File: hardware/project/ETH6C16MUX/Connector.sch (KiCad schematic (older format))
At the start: 3 parts, among them J701 Conn_01x06, J702 Conn_02x09_Odd_Even, J703 C64AC

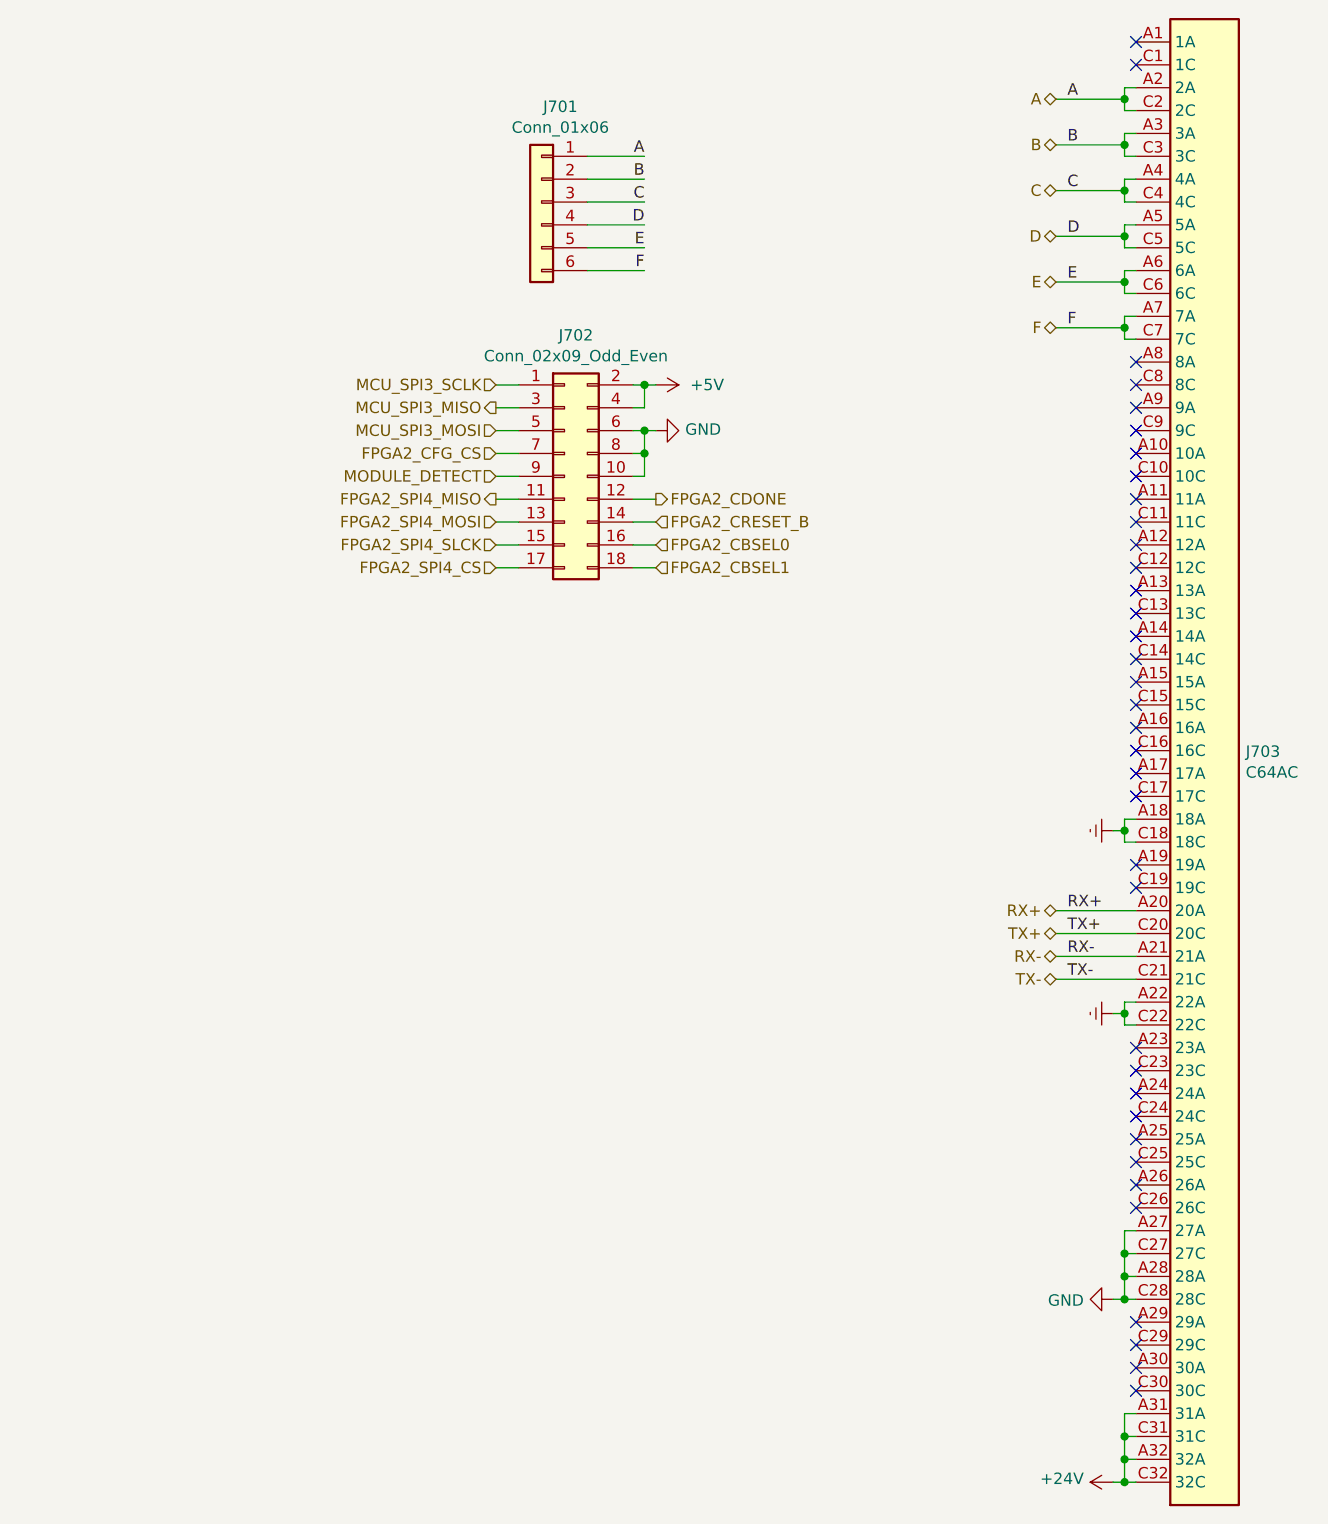
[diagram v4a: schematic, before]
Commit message: Deleted FPGA part and change it for SPI IO chips. Change power supply circuit.
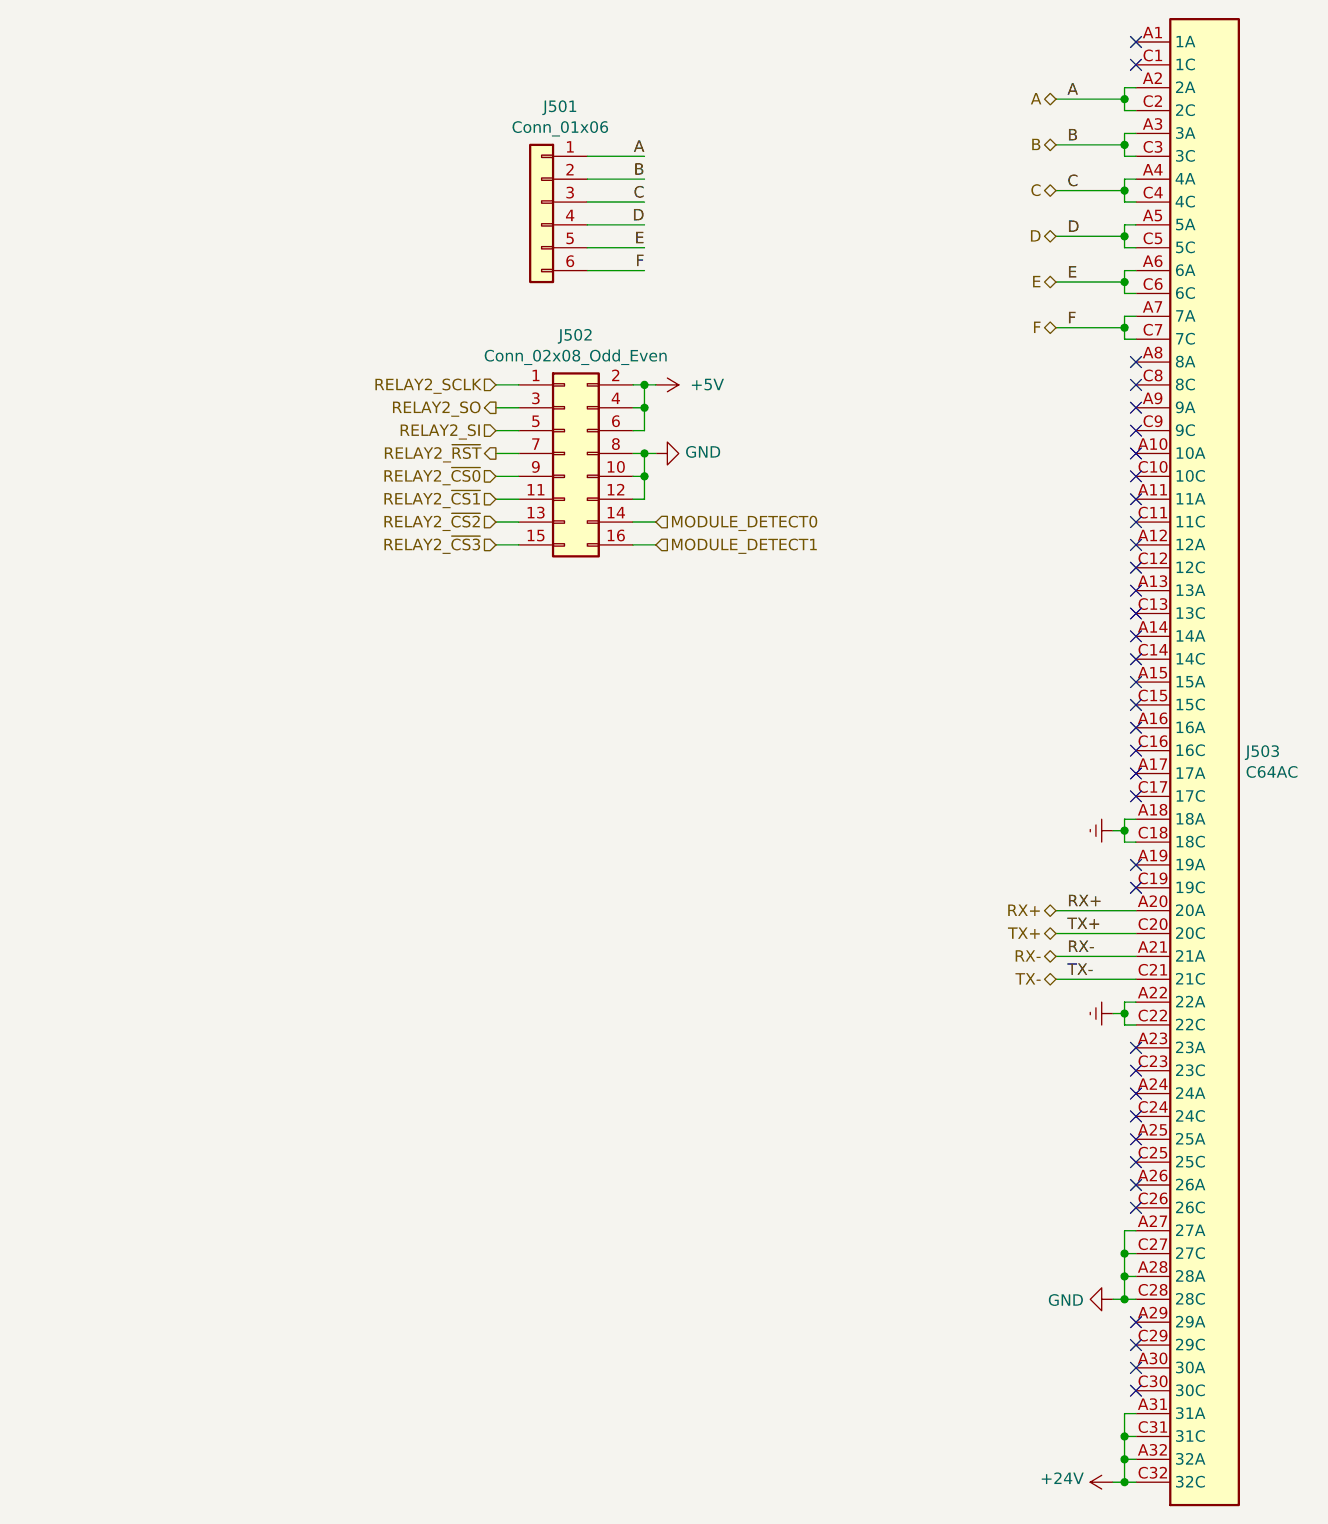
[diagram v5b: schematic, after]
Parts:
- removed J702: Conn_02x09_Odd_Even, Connector_PinSocket_2.54mm:PinSocket_2x09_P2.54mm_Vertical, symbol Connector_Generic:Conn_02x09_Odd_Even
- added J502: Conn_02x08_Odd_Even, Connector_PinSocket_2.54mm:PinSocket_2x08_P2.54mm_Vertical, symbol Connector_Generic:Conn_02x08_Odd_Even
- renumbered J701 to J501, J703 to J503
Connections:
- net +5V: now also J502.2 (Pin_2), J502.4 (Pin_4), J502.6 (Pin_6)
- net GND: now also J502.10 (Pin_10), J502.12 (Pin_12), J502.8 (Pin_8)
- new net MODULE_DETECT0: J502.14 (Pin_14)
- new net MODULE_DETECT1: J502.16 (Pin_16)
- new net RELAY2_SCLK: J502.1 (Pin_1)
- new net RELAY2_SI: J502.5 (Pin_5)
- new net RELAY2_SO: J502.3 (Pin_3)
- new net RELAY2_~CS0: J502.9 (Pin_9)
- new net RELAY2_~CS1: J502.11 (Pin_11)
- new net RELAY2_~CS2: J502.13 (Pin_13)
- new net RELAY2_~CS3: J502.15 (Pin_15)
- new net RELAY2_~RST: J502.7 (Pin_7)
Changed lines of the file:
@@
 $Descr A4 11693 8268
 encoding utf-8
-Sheet 7 7
+Sheet 5 6
 Title ""
 Date ""
@@
 $EndDescr
 $Comp
-L Connector:C64AC J703
+L Connector:C64AC J503
 U 1 1 5DB3A84B
 P 5950 4000
-F 0 "J703" H 6130 4096 50  0000 L CNN
+F 0 "J503" H 6130 4096 50  0000 L CNN
 F 1 "C64AC" H 6130 4005 50  0000 L CNN
 F 2 "ETH6C16MXU:Socket_DIN41612-CaseC1-AC-Male-64Pin-2rows" H 5950 4050 50  0001 C CNN
@@
 	5600 6200 5600 6100
 $Comp
-L power:+24V #PWR0706
+L power:+24V #PWR0506
 U 1 1 5D7D1F7C
 P 5550 7100
-F 0 "#PWR0706" H 5550 6950 50  0001 C CNN
+F 0 "#PWR0506" H 5550 6950 50  0001 C CNN
 F 1 "+24V" V 5565 7228 50  0000 L CNN
 F 2 "" H 5550 7100 50  0001 C CNN
@@
 Connection ~ 5600 7100
 $Comp
-L power:GND #PWR0705
+L power:GND #PWR0505
 U 1 1 5D7D46BE
 P 5550 6300
-F 0 "#PWR0705" H 5550 6050 50  0001 C CNN
+F 0 "#PWR0505" H 5550 6050 50  0001 C CNN
 F 1 "GND" V 5555 6172 50  0000 R CNN
 F 2 "" H 5550 6300 50  0001 C CNN
@@
 RX-
 $Comp
-L power:Earth #PWR0704
+L power:Earth #PWR0504
 U 1 1 5D7F1666
 P 5550 5050
-F 0 "#PWR0704" H 5550 4800 50  0001 C CNN
+F 0 "#PWR0504" H 5550 4800 50  0001 C CNN
 F 1 "Earth" H 5550 4900 50  0001 C CNN
 F 2 "" H 5550 5050 50  0001 C CNN
@@
 	5600 5050 5600 5000
 $Comp
-L power:Earth #PWR0703
+L power:Earth #PWR0503
 U 1 1 5D7F6C0C
 P 5550 4250
-F 0 "#PWR0703" H 5550 4000 50  0001 C CNN
+F 0 "#PWR0503" H 5550 4000 50  0001 C CNN
 F 1 "Earth" H 5550 4100 50  0001 C CNN
 F 2 "" H 5550 4250 50  0001 C CNN
@@
 F
 Wire Wire Line
-	3550 2500 3500 2500
+	3550 2600 3500 2600
+Wire Wire Line
+	3450 2700 3500 2700
+Wire Wire Line
+	3500 2600 3500 2700
+Connection ~ 3500 2600
 Wire Wire Line
 	3450 2600 3500 2600
-Wire Wire Line
-	3500 2500 3500 2600
-Connection ~ 3500 2500
-Wire Wire Line
-	3450 2500 3500 2500
 Wire Wire Line
 	3500 2300 3550 2300
@@
 	2950 2800 2850 2800
 Wire Wire Line
-	2850 3100 2950 3100
-Wire Wire Line
-	2950 3000 2850 3000
-Wire Wire Line
 	2850 2600 2950 2600
 Wire Wire Line
-	3450 3100 3550 3100
-Wire Wire Line
 	3550 3000 3450 3000
 Wire Wire Line
 	3550 2900 3450 2900
 Wire Wire Line
-	3550 2800 3450 2800
-Wire Wire Line
 	2950 2500 2850 2500
 Wire Wire Line
@@
 Wire Wire Line
 	2950 2300 2850 2300
-Text HLabel 2850 2700 0    50   Input ~ 0
-MODULE_DETECT
-$Comp
-L power:GND #PWR0702
+$Comp
+L power:GND #PWR0502
 U 1 1 5D777B58
-P 3550 2500
-AR Path="/5DB25E5A/5D777B58" Ref="#PWR0702"  Part="1"
+P 3550 2600
+AR Path="/5DB25E5A/5D777B58" Ref="#PWR0502"  Part="1"
 AR Path="/5D7599BA/5D777B58" Ref="#PWR?"  Part="1"
-F 0 "#PWR0702" H 3550 2250 50  0001 C CNN
-F 1 "GND" V 3555 2372 50  0000 R CNN
-F 2 "" H 3550 2500 50  0001 C CNN
-F 3 "" H 3550 2500 50  0001 C CNN
-	1    3550 2500
+F 0 "#PWR0502" H 3550 2350 50  0001 C CNN
+F 1 "GND" V 3555 2472 50  0000 R CNN
+F 2 "" H 3550 2600 50  0001 C CNN
+F 3 "" H 3550 2600 50  0001 C CNN
+	1    3550 2600
 	0    -1   -1   0
 $EndComp
 $Comp
-L power:+5V #PWR0701
+L power:+5V #PWR0501
 U 1 1 5D777B5E
 P 3550 2300
-AR Path="/5DB25E5A/5D777B5E" Ref="#PWR0701"  Part="1"
+AR Path="/5DB25E5A/5D777B5E" Ref="#PWR0501"  Part="1"
 AR Path="/5D7599BA/5D777B5E" Ref="#PWR?"  Part="1"
-F 0 "#PWR0701" H 3550 2150 50  0001 C CNN
+F 0 "#PWR0501" H 3550 2150 50  0001 C CNN
 F 1 "+5V" V 3550 2450 50  0000 L CNN
 F 2 "" H 3550 2300 50  0001 C CNN
@@
 	0    1    1    0
 $EndComp
-Text HLabel 2850 2300 0    50   Input ~ 0
-MCU_SPI3_SCLK
-Text HLabel 2850 2400 0    50   Output ~ 0
-MCU_SPI3_MISO
-Text HLabel 2850 2500 0    50   Input ~ 0
-MCU_SPI3_MOSI
-Text HLabel 3550 3000 2    50   Input ~ 0
-FPGA2_CBSEL0
-Text HLabel 3550 3100 2    50   Input ~ 0
-FPGA2_CBSEL1
-Text HLabel 3550 2900 2    50   Input ~ 0
-FPGA2_CRESET_B
-Text HLabel 3550 2800 2    50   Output ~ 0
-FPGA2_CDONE
-Text HLabel 2850 3000 0    50   Input ~ 0
-FPGA2_SPI4_SLCK
-Text HLabel 2850 3100 0    50   Input ~ 0
-FPGA2_SPI4_CS
-Text HLabel 2850 2800 0    50   Output ~ 0
-FPGA2_SPI4_MISO
-Text HLabel 2850 2900 0    50   Input ~ 0
-FPGA2_SPI4_MOSI
-Text HLabel 2850 2600 0    50   Input ~ 0
-FPGA2_CFG_CS
 Text Label 3500 1300 2    50   ~ 0
 A
@@
 P 3050 1500
 AR Path="/5D7599BA/5D777B7C" Ref="J?"  Part="1"
-AR Path="/5DB25E5A/5D777B7C" Ref="J701"  Part="1"
-F 0 "J701" H 2968 1917 50  0000 C CNN
+AR Path="/5DB25E5A/5D777B7C" Ref="J501"  Part="1"
+F 0 "J501" H 2968 1917 50  0000 C CNN
 F 1 "Conn_01x06" H 2968 1826 50  0000 C CNN
 F 2 "Connector_PinSocket_2.54mm:PinSocket_1x06_P2.54mm_Vertical" H 3050 1500 50  0001 C CNN
@@
 Wire Wire Line
 	3250 1800 3500 1800
-$Comp
-L Connector_Generic:Conn_02x09_Odd_Even J702
-U 1 1 5D8AE50E
-P 3150 2700
-F 0 "J702" H 3200 3317 50  0000 C CNN
-F 1 "Conn_02x09_Odd_Even" H 3200 3226 50  0000 C CNN
-F 2 "Connector_PinSocket_2.54mm:PinSocket_2x09_P2.54mm_Vertical" H 3150 2700 50  0001 C CNN
-F 3 "~" H 3150 2700 50  0001 C CNN
-	1    3150 2700
-	1    0    0    -1
-$EndComp
-Wire Wire Line
-	3500 2600 3500 2700
-Wire Wire Line
-	3500 2700 3450 2700
-Connection ~ 3500 2600
+Wire Wire Line
+	3500 2700 3500 2800
+Wire Wire Line
+	3500 2800 3450 2800
+Connection ~ 3500 2700
 NoConn ~ 5650 2200
 NoConn ~ 5650 2300
@@
 NoConn ~ 5650 2600
 NoConn ~ 5650 2700
+Text HLabel 2850 2900 0    50   Input ~ 0
+RELAY2_~CS2
+Text HLabel 2850 2800 0    50   Input ~ 0
+RELAY2_~CS1
+Text HLabel 2850 2700 0    50   Input ~ 0
+RELAY2_~CS0
+Text HLabel 2850 2300 0    50   Input ~ 0
+RELAY2_SCLK
+Text HLabel 2850 2500 0    50   Input ~ 0
+RELAY2_SI
+Text HLabel 2850 2400 0    50   Output ~ 0
+RELAY2_SO
+Text HLabel 2850 2600 0    50   Output ~ 0
+RELAY2_~RST
+Text HLabel 3550 2900 2    50   Input ~ 0
+MODULE_DETECT0
+Text HLabel 3550 3000 2    50   Input ~ 0
+MODULE_DETECT1
+Text HLabel 2850 3000 0    50   Input ~ 0
+RELAY2_~CS3
+Wire Wire Line
+	2850 3000 2950 3000
+Wire Wire Line
+	3450 2500 3500 2500
+Wire Wire Line
+	3500 2500 3500 2400
+Connection ~ 3500 2400
+$Comp
+L Connector_Generic:Conn_02x08_Odd_Even J502
+U 1 1 5F5E8DBC
+P 3150 2600
+F 0 "J502" H 3200 3117 50  0000 C CNN
+F 1 "Conn_02x08_Odd_Even" H 3200 3026 50  0000 C CNN
+F 2 "Connector_PinSocket_2.54mm:PinSocket_2x08_P2.54mm_Vertical" H 3150 2600 50  0001 C CNN
+F 3 "~" H 3150 2600 50  0001 C CNN
+	1    3150 2600
+	1    0    0    -1
+$EndComp
 $EndSCHEMATC
